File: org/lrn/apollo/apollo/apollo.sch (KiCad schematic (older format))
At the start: 40 parts, among them J1 Conn_01x01_Male, J2 Conn_01x01_Male, J3 Conn_01x01_Male, J4 Conn_01x01_Male, Q1 PN2222A, Q2 PN2222A, Q3 PN2222A, Q4 PN2222A, U1 74HC595, U2 5461AS-1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

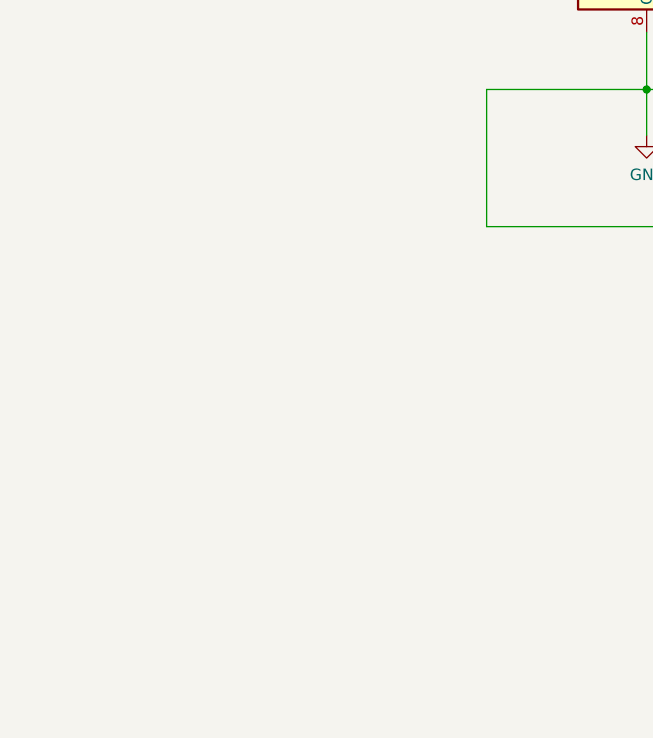
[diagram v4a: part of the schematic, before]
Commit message: apollo: attiny2313 as MCU
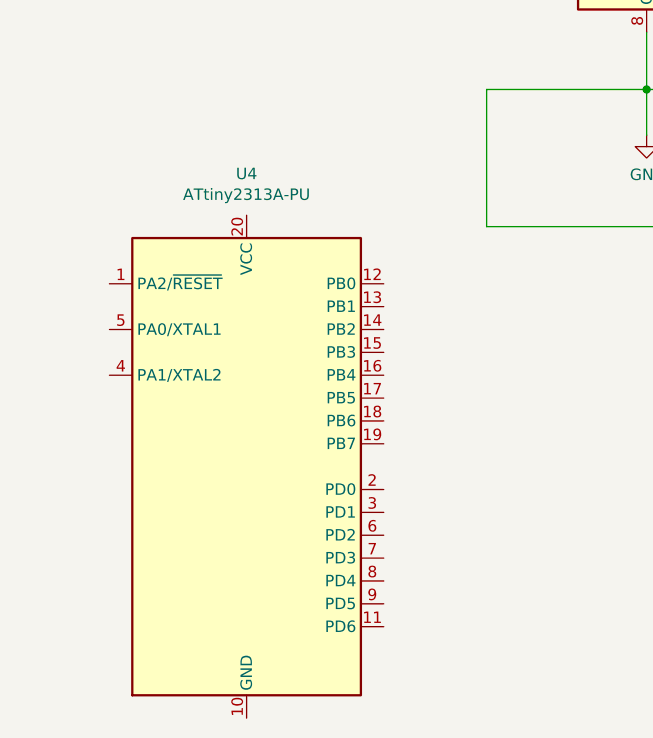
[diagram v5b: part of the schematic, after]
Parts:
- added U4: ATtiny2313A-PU, Package_DIP:DIP-20_W7.62mm, symbol MCU_Microchip_ATtiny:ATtiny2313A-PU
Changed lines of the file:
@@
 Wire Wire Line
 	8900 3100 9400 3100
+$Comp
+L MCU_Microchip_ATtiny:ATtiny2313A-PU U4
+U 1 1 5F59DBF3
+P 1750 7500
+F 0 "U4" H 1750 8781 50  0000 C CNN
+F 1 "ATtiny2313A-PU" H 1750 8690 50  0000 C CNN
+F 2 "Package_DIP:DIP-20_W7.62mm" H 1750 7500 50  0001 C CIN
+F 3 "http://ww1.microchip.com/downloads/en/DeviceDoc/doc8246.pdf" H 1750 7500 50  0001 C CNN
+	1    1750 7500
+	1    0    0    -1
+$EndComp
 $EndSCHEMATC

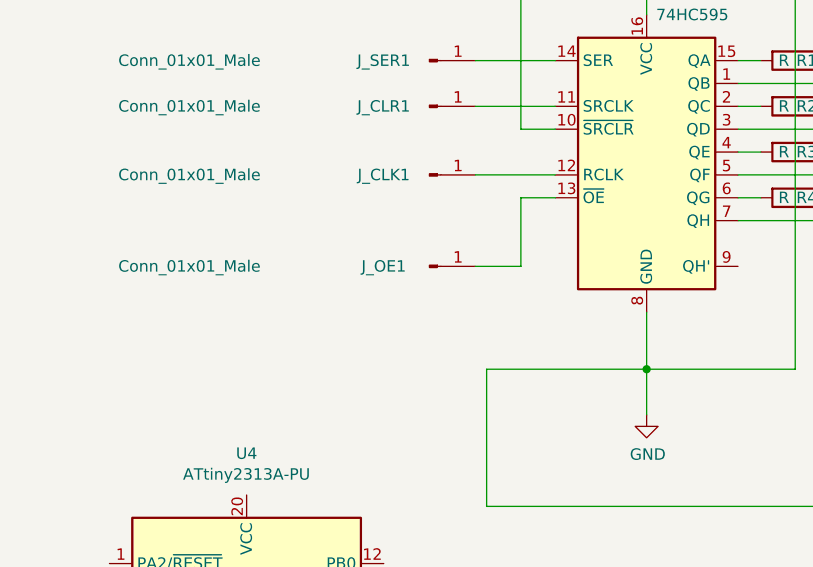
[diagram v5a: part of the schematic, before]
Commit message: apollo: display works w/o timing
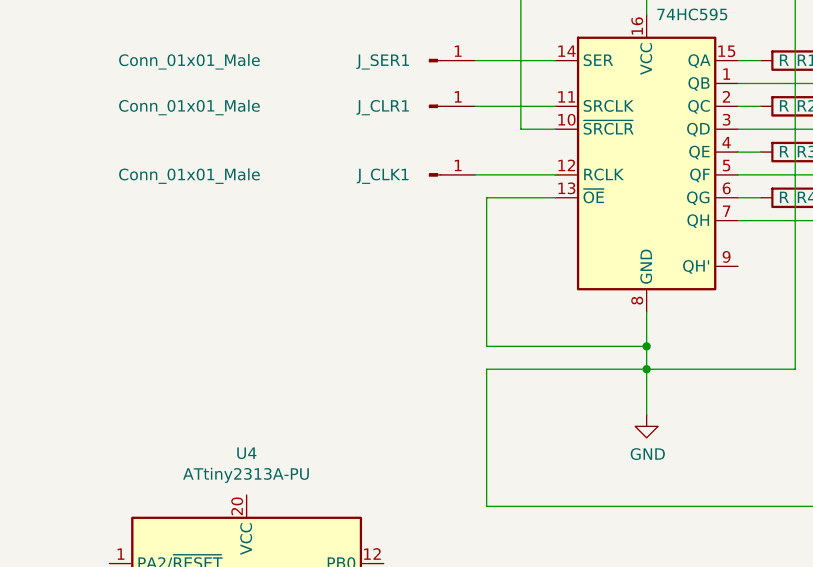
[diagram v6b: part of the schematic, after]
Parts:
- removed J_OE1: Conn_01x01_Male, Connector_Pin:Pin_D0.7mm_L6.5mm_W1.8mm_FlatFork, symbol Connector:Conn_01x01_Male
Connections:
- net GND: now also U1.13 (~OE)
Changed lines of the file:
@@
 	4150 5850 3500 5850
 Wire Wire Line
-	3500 5850 3500 5600
+	3500 5850 3500 5750
 Wire Wire Line
 	6000 3550 4150 3550
@@
 	1    0    0    -1
 $EndComp
-$Comp
-L Connector:Conn_01x01_Male J_OE1
-U 1 1 5F510574
-P 2550 5400
-F 0 "J_OE1" H 2350 5400 50  0000 C CNN
-F 1 "Conn_01x01_Male" H 1500 5400 50  0000 C CNN
-F 2 "Connector_Pin:Pin_D0.7mm_L6.5mm_W1.8mm_FlatFork" H 2550 5400 50  0001 C CNN
-F 3 "~" H 2550 5400 50  0001 C CNN
-	1    2550 5400
-	1    0    0    -1
-$EndComp
-Wire Wire Line
-	3100 5100 2950 5100
-Wire Wire Line
-	2950 5100 2950 5400
-Wire Wire Line
-	2950 5400 2750 5400
 $Comp
 L Connector:Conn_01x01_Male J_CLR1
@@
 	1    0    0    -1
 $EndComp
+Wire Wire Line
+	3100 5100 2800 5100
+Wire Wire Line
+	2800 5100 2800 5750
+Wire Wire Line
+	2800 5750 3500 5750
+Connection ~ 3500 5750
+Wire Wire Line
+	3500 5750 3500 5600
 $EndSCHEMATC

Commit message: apollo: update schematic (draft)
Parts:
- removed U4: ATtiny2313A-PU, Package_DIP:DIP-20_W7.62mm, symbol MCU_Microchip_ATtiny:ATtiny2313A-PU
- added U4: ATmega168P-20PU, Package_DIP:DIP-28_W7.62mm, symbol MCU_Microchip_ATmega:ATmega168P-20PU
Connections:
- net at J_CLR1.1 (Pin_1), U1.11 (SRCLK): now also U4.27 (PC4)
- net at J_CLK1.1 (Pin_1), U1.12 (RCLK): now also U4.28 (PC5)
- net at J_SER1.1 (Pin_1), U1.14 (SER): now also U4.26 (PC3)
- net at J4.1 (Pin_1), Rb4.2: now also U4.23 (PC0)
- net at J3.1 (Pin_1), Rb3.2: now also U4.24 (PC1)
- net at J2.1 (Pin_1), Rb2.2: now also U4.25 (PC2)
- net at J1.1 (Pin_1), Rb1.2: now also U4.15 (PB1)
- new net: U4.22 (GND), U4.8 (GND)
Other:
- moved on the sheet: J1, J2, J3, J4, JA_15, JB_1, JC_2, JDS_14, JD_3, JE_4, JF_5, JG_6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

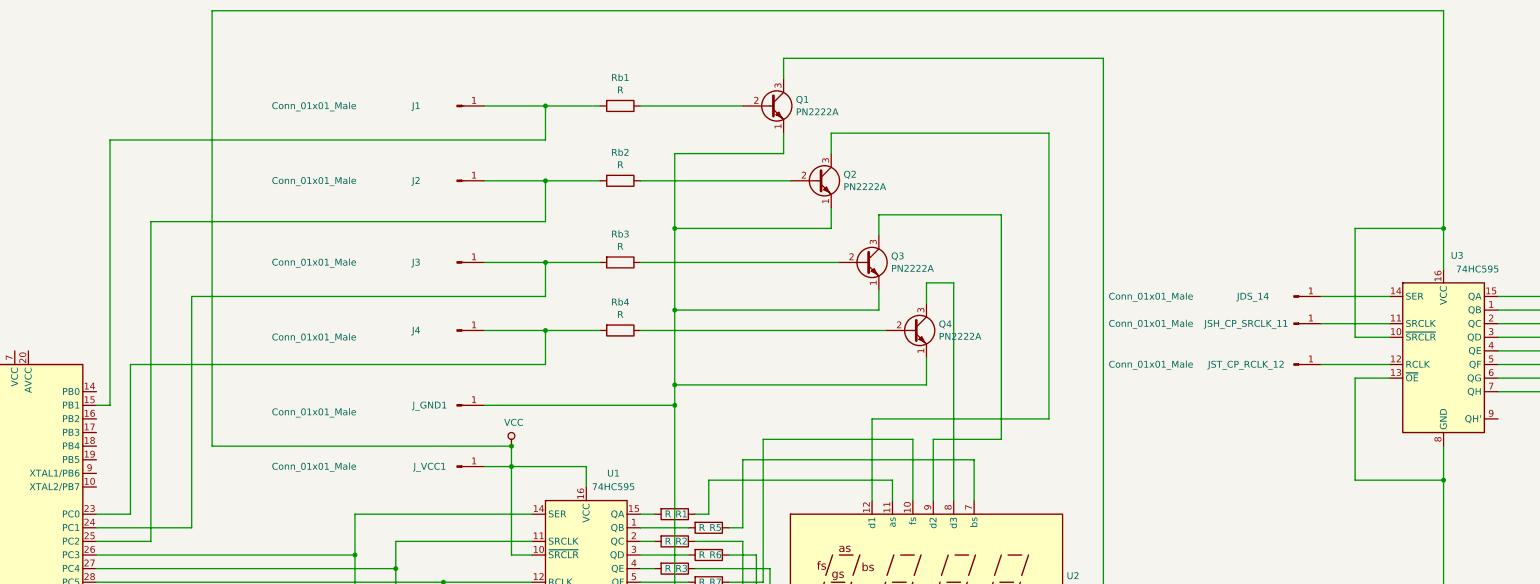
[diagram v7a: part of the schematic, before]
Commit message: apollo: schematic updated
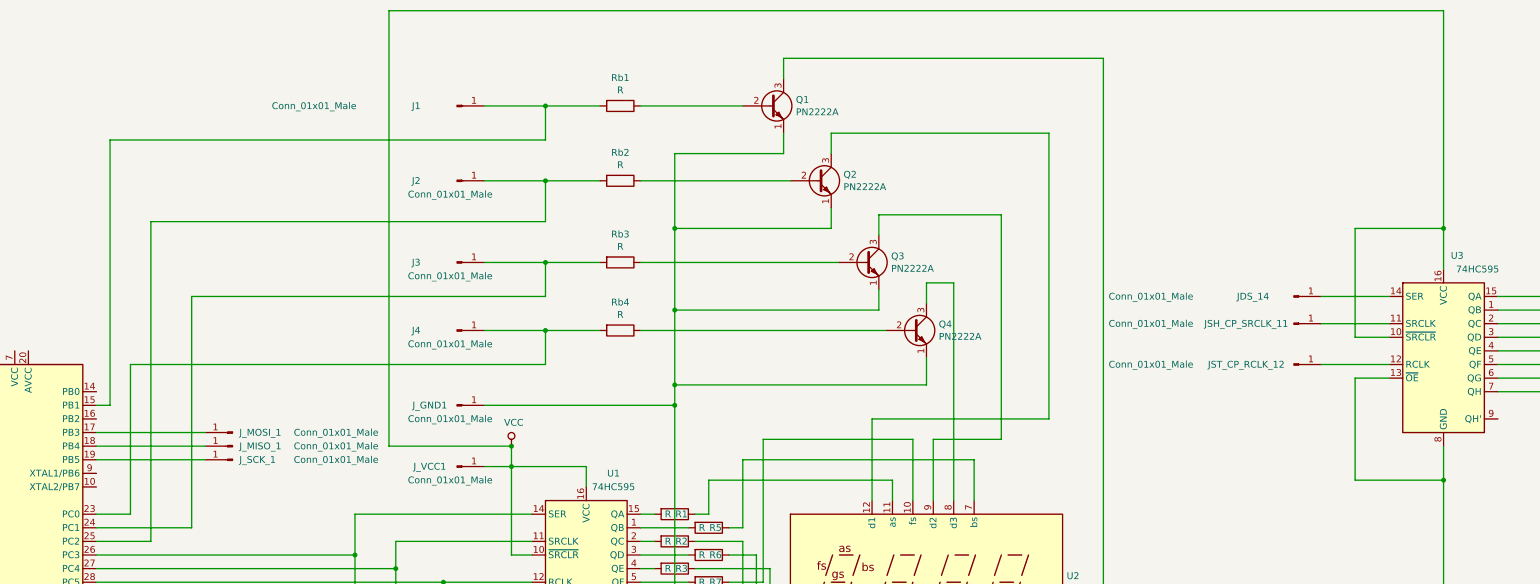
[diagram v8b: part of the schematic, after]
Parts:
- added J_MISO_1, J_MOSI_1, J_SCK_1: Conn_01x01_Male, Connector_Pin:Pin_D0.7mm_L6.5mm_W1.8mm_FlatFork, symbol Connector:Conn_01x01_Male
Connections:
- net at U4.17 (PB3): now also J_MOSI_1.1 (Pin_1)
- net at U4.18 (PB4): now also J_MISO_1.1 (Pin_1)
- net at U4.19 (PB5): now also J_SCK_1.1 (Pin_1)
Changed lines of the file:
@@
 P 3500 12850
 F 0 "J_VCC1" H 3300 12850 50  0000 C CNN
-F 1 "Conn_01x01_Male" H 2450 12850 50  0000 C CNN
+F 1 "Conn_01x01_Male" H 3450 12750 50  0000 C CNN
 F 2 "Connector_Pin:Pin_D0.7mm_L6.5mm_W1.8mm_FlatFork" H 3500 12850 50  0001 C CNN
 F 3 "~" H 3500 12850 50  0001 C CNN
@@
 P 3500 12400
 F 0 "J_GND1" H 3300 12400 50  0000 C CNN
-F 1 "Conn_01x01_Male" H 2450 12350 50  0000 C CNN
+F 1 "Conn_01x01_Male" H 3450 12300 50  0000 C CNN
 F 2 "Connector_Pin:Pin_D0.7mm_L6.5mm_W1.8mm_FlatFork" H 3500 12400 50  0001 C CNN
 F 3 "~" H 3500 12400 50  0001 C CNN
@@
 P 3500 11350
 F 0 "J3" H 3200 11350 50  0000 C CNN
-F 1 "Conn_01x01_Male" H 2450 11350 50  0000 C CNN
+F 1 "Conn_01x01_Male" H 3450 11250 50  0000 C CNN
 F 2 "Connector_Pin:Pin_D0.7mm_L6.5mm_W1.8mm_FlatFork" H 3500 11350 50  0001 C CNN
 F 3 "~" H 3500 11350 50  0001 C CNN
@@
 P 3500 10750
 F 0 "J2" H 3200 10750 50  0000 C CNN
-F 1 "Conn_01x01_Male" H 2450 10750 50  0000 C CNN
+F 1 "Conn_01x01_Male" H 3450 10650 50  0000 C CNN
 F 2 "Connector_Pin:Pin_D0.7mm_L6.5mm_W1.8mm_FlatFork" H 3500 10750 50  0001 C CNN
 F 3 "~" H 3500 10750 50  0001 C CNN
@@
 P 3500 11850
 F 0 "J4" H 3200 11850 50  0000 C CNN
-F 1 "Conn_01x01_Male" H 2450 11800 50  0000 C CNN
+F 1 "Conn_01x01_Male" H 3450 11750 50  0000 C CNN
 F 2 "Connector_Pin:Pin_D0.7mm_L6.5mm_W1.8mm_FlatFork" H 3500 11850 50  0001 C CNN
 F 3 "~" H 3500 11850 50  0001 C CNN
@@
 	10750 12950 10750 12700
 Wire Wire Line
-	3900 12700 1700 12700
-Wire Wire Line
-	1700 12700 1700 9500
-Wire Wire Line
-	1700 9500 10750 9500
+	3900 12700 3000 12700
 Wire Wire Line
 	10750 9500 10750 11100
@@
 	4150 10750 4550 10750
 Wire Wire Line
-	850  13300 1550 13300
-Wire Wire Line
-	1550 13300 1550 11600
-Wire Wire Line
 	1550 11600 4150 11600
 Wire Wire Line
@@
 Wire Wire Line
 	4150 10200 4550 10200
+Wire Wire Line
+	3000 12700 3000 9500
+Wire Wire Line
+	3000 9500 10750 9500
+$Comp
+L Connector:Conn_01x01_Male J_SCK_1
+U 1 1 5F6656CD
+P 1850 12800
+F 0 "J_SCK_1" H 1800 12800 50  0000 R CNN
+F 1 "Conn_01x01_Male" H 1400 12800 50  0000 R CNN
+F 2 "Connector_Pin:Pin_D0.7mm_L6.5mm_W1.8mm_FlatFork" H 1850 12800 50  0001 C CNN
+F 3 "~" H 1850 12800 50  0001 C CNN
+	1    1850 12800
+	-1   0    0    1
+$EndComp
+Wire Wire Line
+	1650 12800 850  12800
+$Comp
+L Connector:Conn_01x01_Male J_MISO_1
+U 1 1 5F66EA40
+P 1850 12700
+F 0 "J_MISO_1" H 1800 12700 50  0000 R CNN
+F 1 "Conn_01x01_Male" H 1400 12700 50  0000 R CNN
+F 2 "Connector_Pin:Pin_D0.7mm_L6.5mm_W1.8mm_FlatFork" H 1850 12700 50  0001 C CNN
+F 3 "~" H 1850 12700 50  0001 C CNN
+	1    1850 12700
+	-1   0    0    1
+$EndComp
+$Comp
+L Connector:Conn_01x01_Male J_MOSI_1
+U 1 1 5F675F94
+P 1850 12600
+F 0 "J_MOSI_1" H 1800 12600 50  0000 R CNN
+F 1 "Conn_01x01_Male" H 1400 12600 50  0000 R CNN
+F 2 "Connector_Pin:Pin_D0.7mm_L6.5mm_W1.8mm_FlatFork" H 1850 12600 50  0001 C CNN
+F 3 "~" H 1850 12600 50  0001 C CNN
+	1    1850 12600
+	-1   0    0    1
+$EndComp
+Wire Wire Line
+	850  12600 1650 12600
+Wire Wire Line
+	850  12700 1650 12700
+Wire Wire Line
+	850  13300 1550 13300
+Wire Wire Line
+	1550 13300 1550 11600
 $EndSCHEMATC
